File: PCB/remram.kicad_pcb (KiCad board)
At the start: 4 copper layers, 140 x 103 mm, 205 parts, among them J1 4DB-P108-06, J10 70543-0002, J11 70543-0002, J12 Conn_02x13_Odd_Even, J13 70543-0002, J14 70543-0002, J15 70543-0002, J16 70543-0003, J17 62201021121, J18 70543-0001, J19 70543-0001, J2 039531-1002, J20 70543-0001, J21 70543-0003, J22 70543-0003, J23 70543-0003, J3 70543-0003, J4 70543-0002, J5 70543-0002, J6 70543-0002, J7 67068-8000, J8 Conn_02x05, J9 Conn_02x05, Q1 PSMN1R8-40YLC,115, Q2 BUK9840-55, Q3 PSMN1R8-40YLC,115, Q4 BUK9840-55, SW1 OS102011MA1QN1, SW2 PTS645VL39-2, U1 TPS54308, U2 AP2112K-3.3TRG1, U3 TMC2130-TA, U4 ADUM4160, U5 STM32F765VIT6, U6 TMC2130-TA, U7 TMC2130-TA, U8 TMC2130-TA, Y1 TSX-3225 24.0000MF15X-AC3

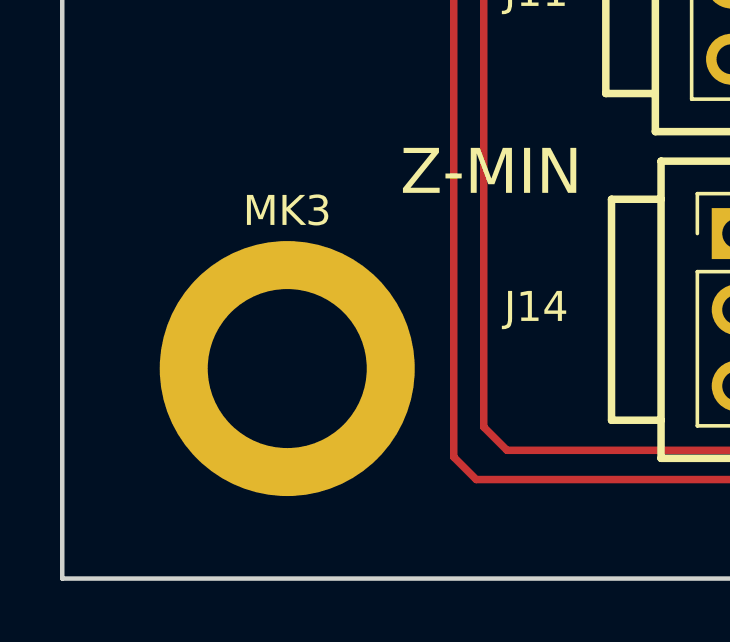
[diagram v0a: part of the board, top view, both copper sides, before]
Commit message: Corrected MK3 hole and added some measurements.
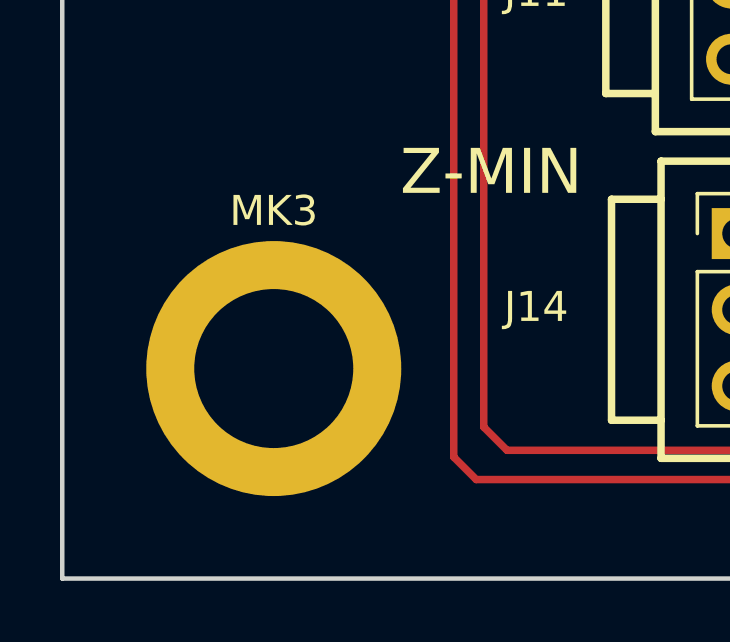
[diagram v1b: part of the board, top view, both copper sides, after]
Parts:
- moved MK3 0.45 mm to (69.2, 137.6)
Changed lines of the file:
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@@
   (general
     (thickness 1.6)
-    (drawings 35)
+    (drawings 43)
     (tracks 2006)
     (zones 0)
@@
   )
   (module MountingHole:MountingHole_5.3mm_M5_ISO14580_Pad (layer F.Cu)
-    (at 69.7 137.55)
+    (at 69.25 137.55)
     (descr "Mounting Hole 5.3mm, M5, ISO14580")
     (tags "mounting hole 5.3mm m5 iso14580")
@@
       (net 1 GND))
   )
+  (dimension 7 (width 0.3) (layer Dwgs.User)
+    (gr_text "7,000 mm" (at 220.6 141 270) (layer Dwgs.User)
+      (effects (font (size 1.5 1.5) (thickness 0.3)))
+    )
+    (feature1 (pts (xy 195.25 144.5) (xy 219.086421 144.5)))
+    (feature2 (pts (xy 195.25 137.5) (xy 219.086421 137.5)))
+    (crossbar (pts (xy 218.5 137.5) (xy 218.5 144.5)))
+    (arrow1a (pts (xy 218.5 144.5) (xy 217.913579 143.373496)))
+    (arrow1b (pts (xy 218.5 144.5) (xy 219.086421 143.373496)))
+    (arrow2a (pts (xy 218.5 137.5) (xy 217.913579 138.626504)))
+    (arrow2b (pts (xy 218.5 137.5) (xy 219.086421 138.626504)))
+  )
+  (dimension 89 (width 0.3) (layer Dwgs.User)
+    (gr_text "89,000 mm" (at 220.6 93 270) (layer Dwgs.User)
+      (effects (font (size 1.5 1.5) (thickness 0.3)))
+    )
+    (feature1 (pts (xy 195.25 137.5) (xy 219.086421 137.5)))
+    (feature2 (pts (xy 195.25 48.5) (xy 219.086421 48.5)))
+    (crossbar (pts (xy 218.5 48.5) (xy 218.5 137.5)))
+    (arrow1a (pts (xy 218.5 137.5) (xy 217.913579 136.373496)))
+    (arrow1b (pts (xy 218.5 137.5) (xy 219.086421 136.373496)))
+    (arrow2a (pts (xy 218.5 48.5) (xy 217.913579 49.626504)))
+    (arrow2b (pts (xy 218.5 48.5) (xy 219.086421 49.626504)))
+  )
+  (dimension 7 (width 0.3) (layer Dwgs.User)
+    (gr_text "7,000 mm" (at 65.75 34.15) (layer Dwgs.User)
+      (effects (font (size 1.5 1.5) (thickness 0.3)))
+    )
+    (feature1 (pts (xy 62.25 48.75) (xy 62.25 35.663579)))
+    (feature2 (pts (xy 69.25 48.75) (xy 69.25 35.663579)))
+    (crossbar (pts (xy 69.25 36.25) (xy 62.25 36.25)))
+    (arrow1a (pts (xy 62.25 36.25) (xy 63.376504 35.663579)))
+    (arrow1b (pts (xy 62.25 36.25) (xy 63.376504 36.836421)))
+    (arrow2a (pts (xy 69.25 36.25) (xy 68.123496 35.663579)))
+    (arrow2b (pts (xy 69.25 36.25) (xy 68.123496 36.836421)))
+  )
+  (dimension 126.000248 (width 0.3) (layer Dwgs.User)
+    (gr_text "126,000 mm" (at 132.221113 34.066225 0.113681953) (layer Dwgs.User)
+      (effects (font (size 1.5 1.5) (thickness 0.3)))
+    )
+    (feature1 (pts (xy 69.25 48.75) (xy 69.224117 35.704801)))
+    (feature2 (pts (xy 195.25 48.5) (xy 195.224117 35.454801)))
+    (crossbar (pts (xy 195.22528 36.041221) (xy 69.22528 36.291221)))
+    (arrow1a (pts (xy 69.22528 36.291221) (xy 70.350618 35.702566)))
+    (arrow1b (pts (xy 69.22528 36.291221) (xy 70.352945 36.875405)))
+    (arrow2a (pts (xy 195.22528 36.041221) (xy 194.097615 35.457037)))
+    (arrow2b (pts (xy 195.22528 36.041221) (xy 194.099942 36.629876)))
+  )
+  (dimension 7 (width 0.3) (layer Dwgs.User)
+    (gr_text "7,000 mm" (at 220.6 45 90) (layer Dwgs.User)
+      (effects (font (size 1.5 1.5) (thickness 0.3)))
+    )
+    (feature1 (pts (xy 195.25 41.5) (xy 219.086421 41.5)))
+    (feature2 (pts (xy 195.25 48.5) (xy 219.086421 48.5)))
+    (crossbar (pts (xy 218.5 48.5) (xy 218.5 41.5)))
+    (arrow1a (pts (xy 218.5 41.5) (xy 219.086421 42.626504)))
+    (arrow1b (pts (xy 218.5 41.5) (xy 217.913579 42.626504)))
+    (arrow2a (pts (xy 218.5 48.5) (xy 219.086421 47.373496)))
+    (arrow2b (pts (xy 218.5 48.5) (xy 217.913579 47.373496)))
+  )
+  (dimension 7 (width 0.3) (layer Dwgs.User)
+    (gr_text "7,000 mm" (at 198.75 33.9) (layer Dwgs.User)
+      (effects (font (size 1.5 1.5) (thickness 0.3)))
+    )
+    (feature1 (pts (xy 202.25 48.5) (xy 202.25 35.413579)))
+    (feature2 (pts (xy 195.25 48.5) (xy 195.25 35.413579)))
+    (crossbar (pts (xy 195.25 36) (xy 202.25 36)))
+    (arrow1a (pts (xy 202.25 36) (xy 201.123496 36.586421)))
+    (arrow1b (pts (xy 202.25 36) (xy 201.123496 35.413579)))
+    (arrow2a (pts (xy 195.25 36) (xy 196.376504 36.586421)))
+    (arrow2b (pts (xy 195.25 36) (xy 196.376504 35.413579)))
+  )
+  (dimension 103.000012 (width 0.3) (layer Dwgs.User)
+    (gr_text "103,000 mm" (at 216.473274 93.04306 -89.97218652) (layer Dwgs.User)
+      (effects (font (size 1.5 1.5) (thickness 0.3)))
+    )
+    (feature1 (pts (xy 202.15 41.55) (xy 214.934694 41.543794)))
+    (feature2 (pts (xy 202.2 144.55) (xy 214.984694 144.543794)))
+    (crossbar (pts (xy 214.398274 144.544079) (xy 214.348274 41.544079)))
+    (arrow1a (pts (xy 214.348274 41.544079) (xy 214.935242 42.670298)))
+    (arrow1b (pts (xy 214.348274 41.544079) (xy 213.7624 42.670867)))
+    (arrow2a (pts (xy 214.398274 144.544079) (xy 214.984148 143.417291)))
+    (arrow2b (pts (xy 214.398274 144.544079) (xy 213.811306 143.41786)))
+  )
+  (dimension 140.000002 (width 0.3) (layer Dwgs.User)
+    (gr_text "140,000 mm" (at 132.198693 151.857339 -0.01023138909) (layer Dwgs.User)
+      (effects (font (size 1.5 1.5) (thickness 0.3)))
+    )
+    (feature1 (pts (xy 62.2 144.525) (xy 62.198963 150.33126)))
+    (feature2 (pts (xy 202.2 144.55) (xy 202.198963 150.35626)))
+    (crossbar (pts (xy 202.199068 149.769839) (xy 62.199068 149.744839)))
+    (arrow1a (pts (xy 62.199068 149.744839) (xy 63.325676 149.158619)))
+    (arrow1b (pts (xy 62.199068 149.744839) (xy 63.325467 150.331461)))
+    (arrow2a (pts (xy 202.199068 149.769839) (xy 201.072669 149.183217)))
+    (arrow2b (pts (xy 202.199068 149.769839) (xy 201.07246 150.356059)))
+  )
   (gr_text "v0.2 - 2018-05-18" (at 134 116) (layer F.SilkS)
     (effects (font (size 1.5 1.5) (thickness 0.3) italic))
@@
   (segment (start 168.05 50.76) (end 168.04 50.75) (width 0.25) (layer B.Cu) (net 18))
   (segment (start 168.05 53.35) (end 168.05 50.76) (width 0.25) (layer B.Cu) (net 18))
+  (segment (start 168.05 69.56) (end 168.04 69.55) (width 0.25) (layer B.Cu) (net 18))
+  (segment (start 168.05 73.15) (end 168.05 69.56) (width 0.25) (layer B.Cu) (net 18))
+  (segment (start 168.04 49.54) (end 168.04 50.75) (width 0.5) (layer F.Cu) (net 18))
+  (segment (start 166.75 48.25) (end 168.04 49.54) (width 0.5) (layer F.Cu) (net 18))
+  (segment (start 163.1 48.25) (end 166.75 48.25) (width 0.5) (layer F.Cu) (net 18))
+  (segment (start 161.5 50.8) (end 161.5 49.85) (width 0.5) (layer F.Cu) (net 18))
+  (segment (start 161.5 49.85) (end 163.1 48.25) (width 0.5) (layer F.Cu) (net 18))
+  (segment (start 168.05 69.54) (end 168.04 69.55) (width 0.5) (layer F.Cu) (net 18))
+  (segment (start 168.05 68.3) (end 168.05 69.54) (width 0.5) (layer F.Cu) (net 18))
+  (segment (start 166.8 67.05) (end 168.05 68.3) (width 0.5) (layer F.Cu) (net 18))
+  (segment (start 163.3 67.05) (end 166.8 67.05) (width 0.5) (layer F.Cu) (net 18))
+  (segment (start 161.5 69.6) (end 161.5 68.85) (width 0.5) (layer F.Cu) (net 18))
+  (segment (start 161.5 68.85) (end 163.3 67.05) (width 0.5) (layer F.Cu) (net 18))
   (segment (start 87.94 52.61) (end 87.95 52.6) (width 0.25) (layer B.Cu) (net 21) (status 30))
   (via (at 80.8 64.799996) (size 0.8) (drill 0.4) (layers F.Cu B.Cu) (net 21))
@@
   (via (at 137 63.8) (size 0.8) (drill 0.4) (layers F.Cu B.Cu) (net 70))
   (via (at 158 63.8) (size 0.8) (drill 0.4) (layers F.Cu B.Cu) (net 70))
-  (segment (start 168.05 69.56) (end 168.04 69.55) (width 0.25) (layer B.Cu) (net 18))
-  (segment (start 168.05 73.15) (end 168.05 69.56) (width 0.25) (layer B.Cu) (net 18))
-  (segment (start 168.04 49.54) (end 168.04 50.75) (width 0.5) (layer F.Cu) (net 18))
-  (segment (start 166.75 48.25) (end 168.04 49.54) (width 0.5) (layer F.Cu) (net 18))
-  (segment (start 163.1 48.25) (end 166.75 48.25) (width 0.5) (layer F.Cu) (net 18))
-  (segment (start 161.5 50.8) (end 161.5 49.85) (width 0.5) (layer F.Cu) (net 18))
-  (segment (start 161.5 49.85) (end 163.1 48.25) (width 0.5) (layer F.Cu) (net 18))
-  (segment (start 168.05 69.54) (end 168.04 69.55) (width 0.5) (layer F.Cu) (net 18))
-  (segment (start 168.05 68.3) (end 168.05 69.54) (width 0.5) (layer F.Cu) (net 18))
-  (segment (start 166.8 67.05) (end 168.05 68.3) (width 0.5) (layer F.Cu) (net 18))
-  (segment (start 163.3 67.05) (end 166.8 67.05) (width 0.5) (layer F.Cu) (net 18))
-  (segment (start 161.5 69.6) (end 161.5 68.85) (width 0.5) (layer F.Cu) (net 18))
-  (segment (start 161.5 68.85) (end 163.3 67.05) (width 0.5) (layer F.Cu) (net 18))
   (via (at 118.45 132.05) (size 1) (drill 0.6) (layers F.Cu B.Cu) (net 70))
   (segment (start 118.45 126.81) (end 118.43 126.79) (width 1) (layer F.Cu) (net 70))

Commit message: Version 0.3.
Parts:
- removed the C10 at (169.7, 118.0)
- removed the C28 at (136.2, 98.1)
- added C11: 100nF, Capacitor_SMD:C_1812_4532Metric, F.Cu at (169.7, 118.0)
- added C29: 8pF, Capacitor_SMD:C_0603_1608Metric, F.Cu at (136.2, 99.9)
- added C8: 100uF, Capacitor_THT:CP_Radial_D6.3mm_P2.50mm, F.Cu at (183.7, 135.6)
- C3: footprint Capacitor_SMD:C_0603_1608Metric -> Capacitor_SMD:C_1206_3216Metric
- moved D2 7.46 mm to (187.2, 140.3), turned to 0 degrees
- moved D3 0.85 mm to (175.6, 118.0)
- moved C9 0.58 mm to (177.4, 134.5)
- moved C3 0.49 mm to (160.9, 130.1)
- renumbered C9 to C10, C11 to C12, C12 to C13, C13 to C14, C14 to C15, C15 to C16, C16 to C17, C17 to C18, C18 to C19, C19 to C20, C20 to C21, C21 to C22, C22 to C23, C23 to C24, C24 to C25, C25 to C26, C26 to C27, C27 to C28, C29 to C30, C30 to C31, C31 to C32, C32 to C33, C33 to C34, C34 to C35, C35 to C36, C36 to C37, C37 to C38, C38 to C39, C39 to C40, C40 to C41, C41 to C42, C42 to C43, C43 to C44, C44 to C45, C45 to C46, C46 to C47, C47 to C48, C48 to C49, C49 to C50, C50 to C51, C51 to C52, C52 to C53, C53 to C54, C54 to C55, C55 to C56, C56 to C57, C57 to C58, C58 to C59, C59 to C60, C60 to C61, C61 to C62, C62 to C63, C63 to C64, C64 to C65, C65 to C66, C66 to C67, C67 to C68, C68 to C69, C69 to C70, C70 to C71, C71 to C72, C8 to C9
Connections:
- U5 pad 12: Net-(C28-Pad1) -> Net-(C29-Pad1)
- Y1 pad 2: Net-(C28-Pad1) -> GND
- Y1 pad 3: (no net) -> Net-(C29-Pad1)
- Y1 pad 4: (no net) -> GND
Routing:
- net Net-(C29-Pad1): track 0.00 -> 14.0 mm
- net Net-(C28-Pad1): track 13.6 -> 0.00 mm
- net GND: track 218.1 -> 220.9 mm, vias 112 -> 114
- net Net-(C28-Pad2): track 16.6 -> 18.1 mm
- net VDD_PWR: track 170.6 -> 169.9 mm
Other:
- board text added: "v0.3 - 2018-05-18"
- board text removed: "v0.2 - 2018-05-18"

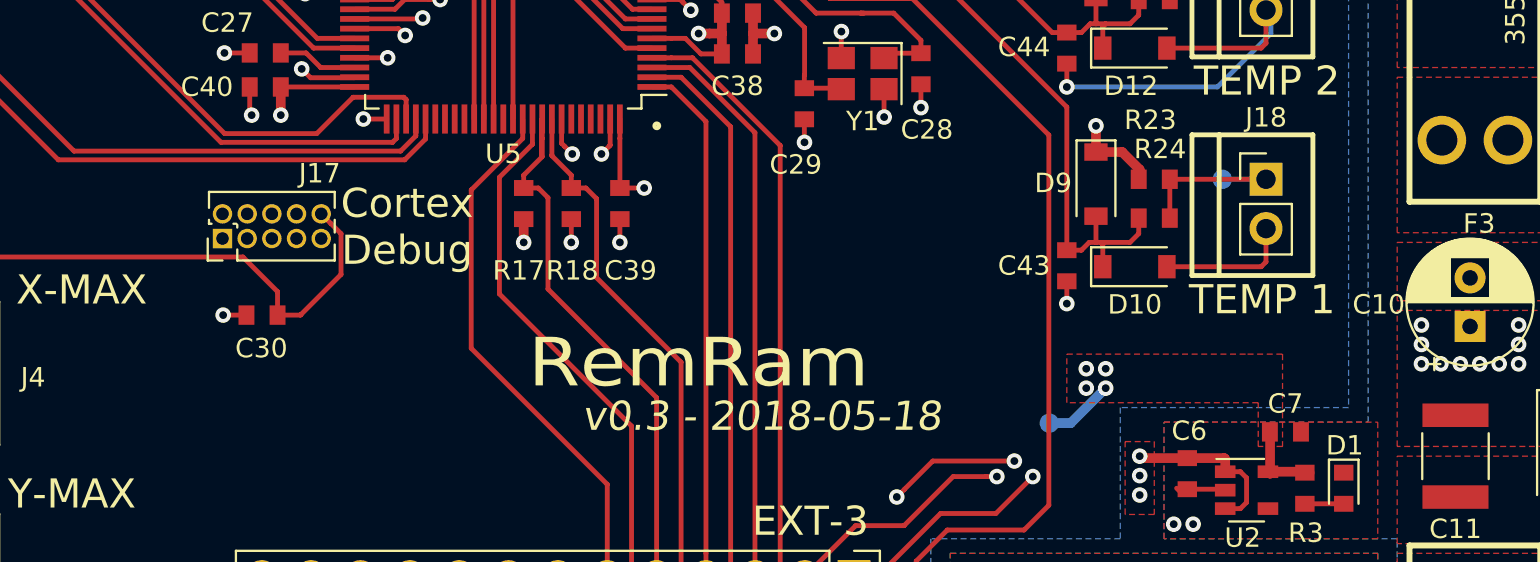
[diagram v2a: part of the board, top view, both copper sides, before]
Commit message: Added a yellow status LED.
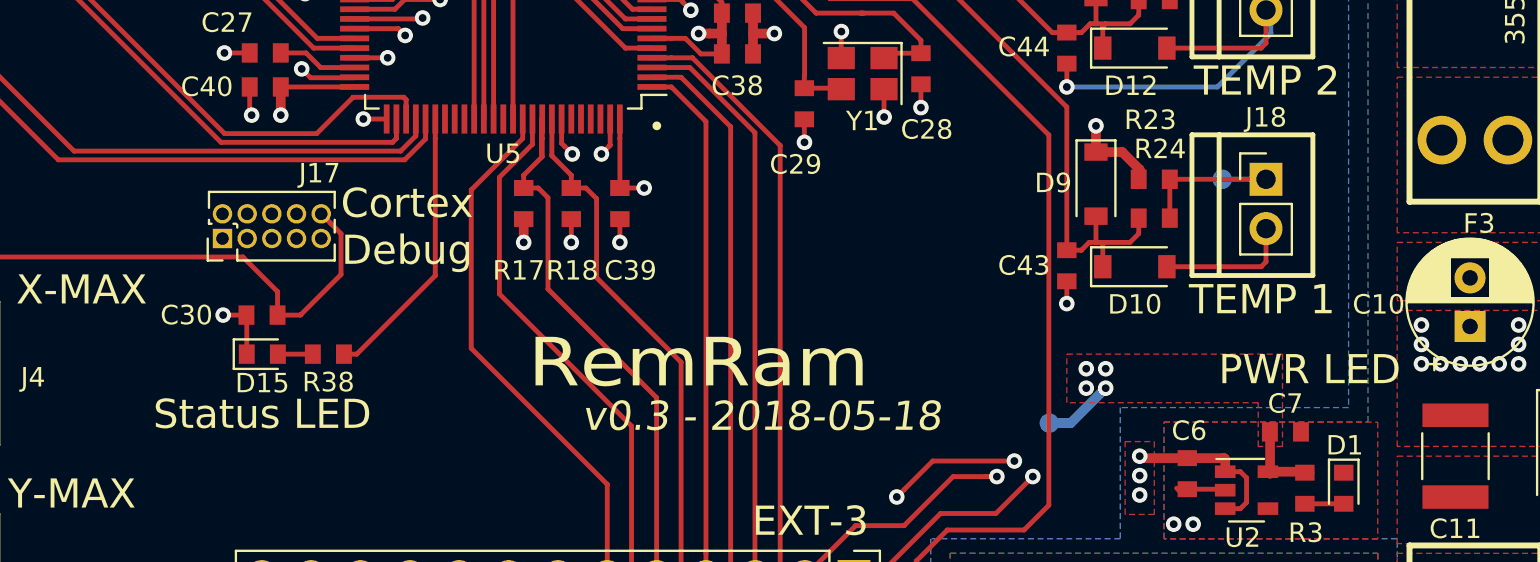
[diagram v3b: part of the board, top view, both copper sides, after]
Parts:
- added D15: LTST-C194KSKT, LED_SMD:LED_0603_1608Metric, F.Cu at (108.3, 112.8)
- added R38: 1k, Resistor_SMD:R_0603_1608Metric, F.Cu at (111.7, 112.8)
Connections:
- U5 pad 81: Net-(U5-Pad81) -> /MCU/STATUS_LED
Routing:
- net /MCU/STATUS_LED: track 0.00 -> 14.4 mm
- net GND: track 220.9 -> 222.9 mm
- net Net-(D15-Pad2): track 0.00 -> 1.80 mm
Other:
- board text added: "PWR LED"
- board text added: "Status LED"

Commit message: Changed the LED resistors to real values.
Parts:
- R3, R38: value 1k -> 68
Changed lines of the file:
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@@
       (effects (font (size 1 1) (thickness 0.15)))
     )
-    (fp_text value 1k (at 0 1.45 180) (layer F.Fab)
+    (fp_text value 68 (at 0 1.45 180) (layer F.Fab)
       (effects (font (size 1 1) (thickness 0.15)))
     )
@@
       (effects (font (size 1 1) (thickness 0.15)))
     )
-    (fp_text value 1k (at 0 1.45 270) (layer F.Fab)
+    (fp_text value 68 (at 0 1.45 270) (layer F.Fab)
       (effects (font (size 1 1) (thickness 0.15)))
     )

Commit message: Changed ordering of parts. Version 0.4.
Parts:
- renumbered C23 to C14, C24 to C15, C25 to C16, C26 to C17, C27 to C18, C28 to C19, C29 to C20, C30 to C21, C31 to C22, C32 to C23, C33 to C24, C34 to C25, C35 to C26, C36 to C27, C37 to C28, C38 to C29, C39 to C30, C40 to C31, C41 to C32, C42 to C33, C43 to C34, C44 to C35, C45 to C36, C14 to C37, C15 to C38, C16 to C39, C17 to C40, C18 to C41, C19 to C42, C20 to C43, C21 to C44, C22 to C45, C55 to C46, C56 to C47, C57 to C48, C58 to C49, C59 to C50, C60 to C51, C61 to C52, C62 to C53, C63 to C54, C64 to C55, C65 to C56, C66 to C57, C67 to C58, C68 to C59, C69 to C60, C70 to C61, C71 to C62, C72 to C63, C46 to C64, C47 to C65, C48 to C66, C49 to C67, C50 to C68, C51 to C69, C52 to C70, C53 to C71, C54 to C72, D9 to D10, D10 to D11, D11 to D12, D12 to D13, D13 to D14, D14 to D15, D15 to D9, J11 to J10, J12 to J11, J13 to J12, J14 to J13, J15 to J14, J16 to J15, J17 to J16, J18 to J17, J19 to J18, J20 to J19, J3 to J20, J22 to J21, J23 to J22, J21 to J23, J4 to J3, J5 to J4, J6 to J5, J7 to J6, J8 to J7, J9 to J8, J10 to J9, R15 to R12, R16 to R13, R17 to R14, R18 to R15, R19 to R16, R20 to R17, R21 to R18, R22 to R19, R38 to R20, R23 to R21, R24 to R22, R25 to R23, R26 to R24, R27 to R25, R28 to R26, R12 to R27, R13 to R28, R14 to R29, R32 to R30, R33 to R31, R34 to R32, R35 to R33, R36 to R34, R37 to R35, R29 to R36, R30 to R37, R31 to R38, TP15 to TP11, TP16 to TP12, TP17 to TP13, TP18 to TP14, TP19 to TP15, TP20 to TP16, TP21 to TP17, TP22 to TP18, TP23 to TP19, TP11 to TP20, TP12 to TP21, TP13 to TP22, TP14 to TP23, TP28 to TP24, TP29 to TP25, TP30 to TP26, TP31 to TP27, TP32 to TP28, TP33 to TP29, TP34 to TP30, TP35 to TP31, TP24 to TP32, TP25 to TP33, TP26 to TP34, TP27 to TP35, U4 to U3, U5 to U4, U3 to U5, U7 to U6, U8 to U7, U6 to U8
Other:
- board text added: "v0.4 - 2018-05-19"
- board text removed: "v0.3 - 2018-05-18"

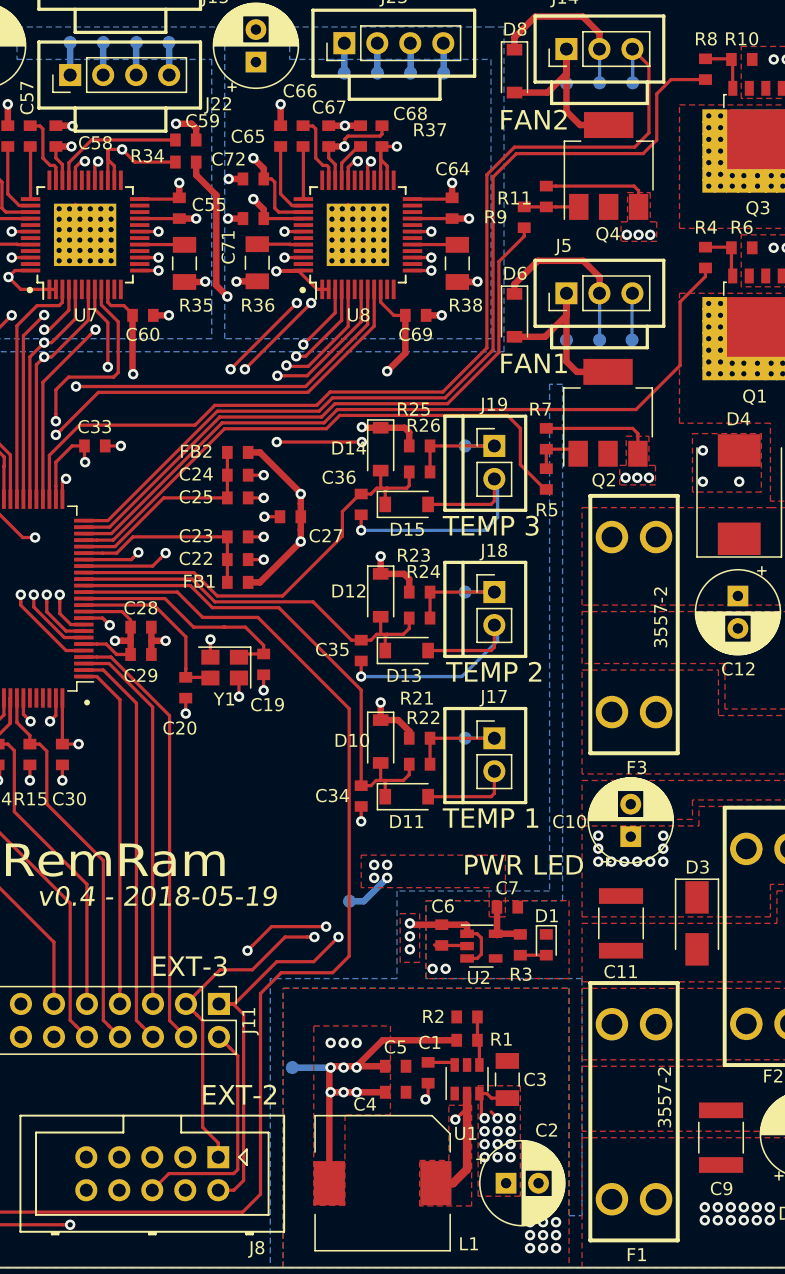
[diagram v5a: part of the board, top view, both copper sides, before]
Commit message: Moved some ADC lines for better noise isolation.
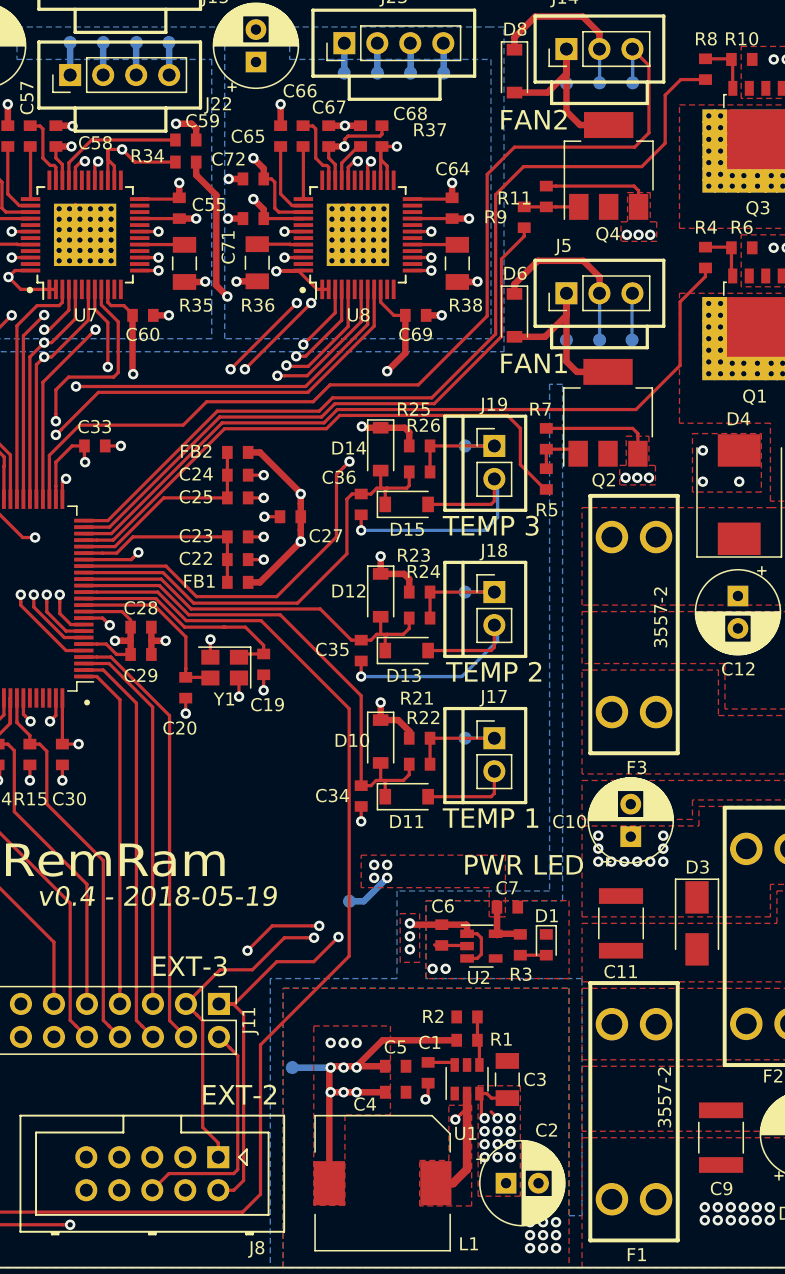
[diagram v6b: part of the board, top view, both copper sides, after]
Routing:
- net /MCU/FAN_SPEED1: track 54.5 -> 59.3 mm, vias 3 -> 1
- net /MCU/nRESET: track 224.2 -> 221.9 mm
- net /MCU/THERM_3: track 34.3 -> 36.1 mm
- net /MCU/FAN_SPEED2: track 77.2 -> 75.8 mm
- net /MCU/PWM_HEAT: track 71.8 -> 70.4 mm
- net /MCU/MOSI: track 173.9 -> 173.1 mm
- net /MCU/PWM_FAN2: track 47.9 -> 47.3 mm
